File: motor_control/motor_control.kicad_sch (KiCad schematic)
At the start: 20 parts, among them J1 GPIO, J2 Conn_01x06_Pin, J3 Conn_01x06_Pin, SW1 PULLUP, SW2 PULLDOWN, SW4 SW_SPST, U1 HC-SR04

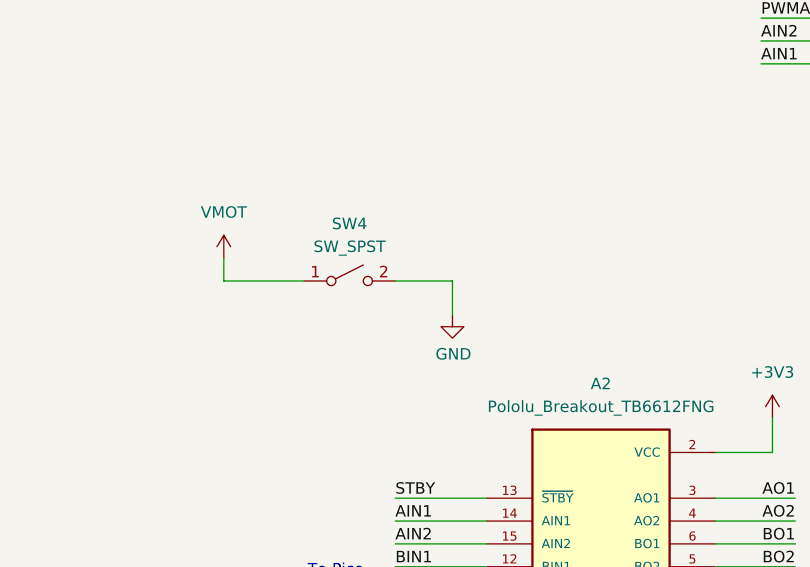
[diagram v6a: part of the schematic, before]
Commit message: replace tb6612 power switch with a 01x02 pin header
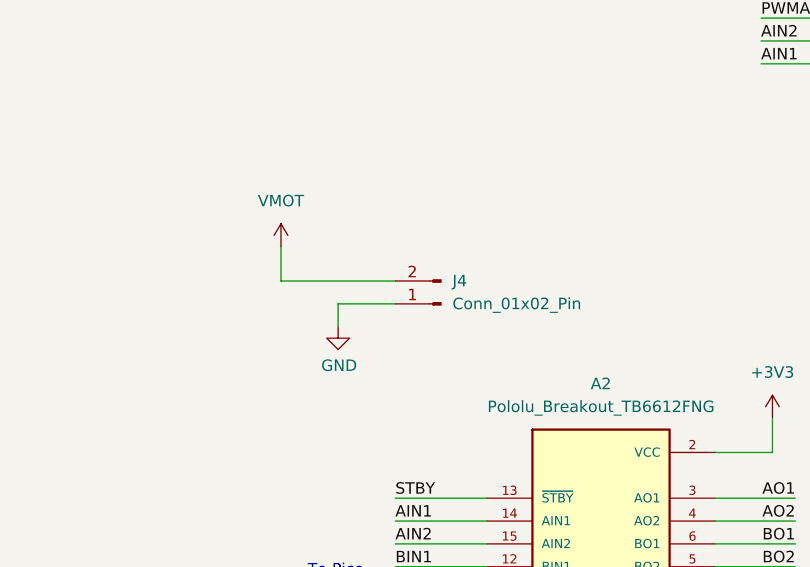
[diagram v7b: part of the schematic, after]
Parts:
- removed SW4: SW_SPST, symbol Switch:SW_SPST
- added J4: Conn_01x02_Pin, symbol Connector:Conn_01x02_Pin
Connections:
- net GND: now also J4.1 (Pin_1)
- net VMOT: now also J4.2 (Pin_2)
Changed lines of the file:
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@@
 	(wire
 		(pts
-			(xy 132.08 106.68) (xy 132.08 109.22)
-		)
-		(stroke
-			(width 0)
-			(type default)
-		)
-	)
-	(wire
-		(pts
 			(xy 76.2 50.8) (xy 76.2 63.5)
 		)
@@
 	(wire
 		(pts
+			(xy 151.13 111.76) (xy 144.78 111.76)
+		)
+		(stroke
+			(width 0)
+			(type default)
+		)
+	)
+	(wire
+		(pts
 			(xy 251.46 77.47) (xy 264.16 77.47)
 		)
@@
 	(wire
 		(pts
+			(xy 138.43 109.22) (xy 151.13 109.22)
+		)
+		(stroke
+			(width 0)
+			(type default)
+		)
+	)
+	(wire
+		(pts
 			(xy 142.24 151.13) (xy 161.29 151.13)
 		)
@@
 	(wire
 		(pts
+			(xy 144.78 111.76) (xy 144.78 114.3)
+		)
+		(stroke
+			(width 0)
+			(type default)
+		)
+	)
+	(wire
+		(pts
 			(xy 55.88 48.26) (xy 60.96 48.26)
 		)
@@
 	(wire
 		(pts
-			(xy 151.13 109.22) (xy 157.48 109.22)
-		)
-		(stroke
-			(width 0)
-			(type default)
-		)
-	)
-	(wire
-		(pts
-			(xy 157.48 109.22) (xy 157.48 113.03)
-		)
-		(stroke
-			(width 0)
-			(type default)
-		)
-	)
-	(wire
-		(pts
 			(xy 87.63 151.13) (xy 95.25 151.13)
 		)
@@
 	(wire
 		(pts
-			(xy 132.08 109.22) (xy 140.97 109.22)
-		)
-		(stroke
-			(width 0)
-			(type default)
-		)
-	)
-	(wire
-		(pts
 			(xy 31.75 53.34) (xy 60.96 53.34)
 		)
@@
 	(wire
 		(pts
+			(xy 138.43 105.41) (xy 138.43 109.22)
+		)
+		(stroke
+			(width 0)
+			(type default)
+		)
+	)
+	(wire
+		(pts
 			(xy 58.42 76.2) (xy 60.96 76.2)
 		)
@@
 	(symbol
 		(lib_id "power:+3V3")
-		(at 132.08 106.68 0)
-		(unit 1)
-		(exclude_from_sim no)
-		(in_bom yes)
-		(on_board yes)
-		(dnp no)
-		(fields_autoplaced yes)
-		(property "Reference" "#PWR021"
-			(at 132.08 110.49 0)
-			(effects
-				(font
-					(size 1.27 1.27)
-				)
-				(hide yes)
-			)
-		)
-		(property "Value" "VMOT"
-			(at 132.08 101.6 0)
-			(effects
-				(font
-					(size 1.27 1.27)
-				)
-			)
-		)
-		(property "Footprint" ""
-			(at 132.08 106.68 0)
-			(effects
-				(font
-					(size 1.27 1.27)
-				)
-				(hide yes)
-			)
-		)
-		(property "Datasheet" ""
-			(at 132.08 106.68 0)
-			(effects
-				(font
-					(size 1.27 1.27)
-				)
-				(hide yes)
-			)
-		)
-		(property "Description" "Power symbol creates a global label with name \"+3V3\""
-			(at 132.08 106.68 0)
-			(effects
-				(font
-					(size 1.27 1.27)
-				)
-				(hide yes)
-			)
-		)
-		(pin "1"
-		)
-		(instances
-			(project "motor_control"
-				(path "/e63e39d7-6ac0-4ffd-8aa3-1841a4541b55"
-					(reference "#PWR021")
-					(unit 1)
-				)
-			)
-		)
-	)
-	(symbol
-		(lib_id "power:+3V3")
 		(at 63.5 128.27 0)
 		(unit 1)
@@
 	)
 	(symbol
+		(lib_id "Connector:Conn_01x02_Pin")
+		(at 156.21 111.76 180)
+		(unit 1)
+		(exclude_from_sim no)
+		(in_bom yes)
+		(on_board yes)
+		(dnp no)
+		(fields_autoplaced yes)
+		(property "Reference" "J4"
+			(at 157.48 109.2199 0)
+			(effects
+				(font
+					(size 1.27 1.27)
+				)
+				(justify right)
+			)
+		)
+		(property "Value" "Conn_01x02_Pin"
+			(at 157.48 111.7599 0)
+			(effects
+				(font
+					(size 1.27 1.27)
+				)
+				(justify right)
+			)
+		)
+		(property "Footprint" ""
+			(at 156.21 111.76 0)
+			(effects
+				(font
+					(size 1.27 1.27)
+				)
+				(hide yes)
+			)
+		)
+		(property "Datasheet" "~"
+			(at 156.21 111.76 0)
+			(effects
+				(font
+					(size 1.27 1.27)
+				)
+				(hide yes)
+			)
+		)
+		(property "Description" "Generic connector, single row, 01x02, script generated"
+			(at 156.21 111.76 0)
+			(effects
+				(font
+					(size 1.27 1.27)
+				)
+				(hide yes)
+			)
+		)
+		(pin "1"
+		)
+		(pin "2"
+		)
+		(instances
+			(project ""
+				(path "/e63e39d7-6ac0-4ffd-8aa3-1841a4541b55"
+					(reference "J4")
+					(unit 1)
+				)
+			)
+		)
+	)
+	(symbol
 		(lib_id "Device:LED_RKGB")
 		(at 107.95 179.07 180)
@@
 	)
 	(symbol
-		(lib_id "power:+3V3")
-		(at 223.52 19.05 0)
+		(lib_id "power:GND")
+		(at 144.78 114.3 0)
 		(unit 1)
 		(exclude_from_sim no)
@@
 		(on_board yes)
 		(dnp no)
-		(fields_autoplaced yes)
-		(property "Reference" "#PWR014"
-			(at 223.52 22.86 0)
+		(property "Reference" "#PWR021"
+			(at 144.78 120.65 0)
 			(effects
 				(font
@@
 			)
 		)
-		(property "Value" "VSYS"
-			(at 223.52 13.97 0)
+		(property "Value" "GND"
+			(at 144.8943 118.6244 0)
 			(effects
 				(font
@@
 		)
 		(property "Footprint" ""
-			(at 223.52 19.05 0)
+			(at 144.78 114.3 0)
 			(effects
 				(font
 					(size 1.27 1.27)
 				)
-				(hide yes)
 			)
 		)
 		(property "Datasheet" ""
-			(at 223.52 19.05 0)
+			(at 144.78 114.3 0)
 			(effects
 				(font
 					(size 1.27 1.27)
 				)
-				(hide yes)
 			)
 		)
-		(property "Description" "Power symbol creates a global label with name \"+3V3\""
-			(at 223.52 19.05 0)
+		(property "Description" "Power symbol creates a global label with name \"GND\" , ground"
+			(at 144.78 114.3 0)
 			(effects
 				(font
@@
 			(project "motor_control"
 				(path "/e63e39d7-6ac0-4ffd-8aa3-1841a4541b55"
-					(reference "#PWR014")
+					(reference "#PWR021")
 					(unit 1)
 				)
@@
 	)
 	(symbol
-		(lib_id "Switch:SW_SPST")
-		(at 146.05 109.22 0)
+		(lib_id "power:+3V3")
+		(at 223.52 19.05 0)
 		(unit 1)
 		(exclude_from_sim no)
@@
 		(dnp no)
 		(fields_autoplaced yes)
-		(property "Reference" "SW4"
-			(at 146.05 102.87 0)
+		(property "Reference" "#PWR014"
+			(at 223.52 22.86 0)
 			(effects
 				(font
 					(size 1.27 1.27)
 				)
+				(hide yes)
 			)
 		)
-		(property "Value" "SW_SPST"
-			(at 146.05 105.41 0)
+		(property "Value" "VSYS"
+			(at 223.52 13.97 0)
 			(effects
 				(font
@@
 		)
 		(property "Footprint" ""
-			(at 146.05 109.22 0)
+			(at 223.52 19.05 0)
 			(effects
 				(font
@@
 			)
 		)
-		(property "Datasheet" "~"
-			(at 146.05 109.22 0)
+		(property "Datasheet" ""
+			(at 223.52 19.05 0)
 			(effects
 				(font
@@
 			)
 		)
-		(property "Description" "Single Pole Single Throw (SPST) switch"
-			(at 146.05 109.22 0)
+		(property "Description" "Power symbol creates a global label with name \"+3V3\""
+			(at 223.52 19.05 0)
 			(effects
 				(font
@@
 			)
 		)
-		(pin "2"
-		)
 		(pin "1"
 		)
 		(instances
-			(project ""
+			(project "motor_control"
 				(path "/e63e39d7-6ac0-4ffd-8aa3-1841a4541b55"
-					(reference "SW4")
+					(reference "#PWR014")
 					(unit 1)
 				)
@@
 	)
 	(symbol
-		(lib_id "power:GND")
-		(at 157.48 113.03 0)
+		(lib_id "power:+3V3")
+		(at 138.43 105.41 0)
 		(unit 1)
 		(exclude_from_sim no)
@@
 		(on_board yes)
 		(dnp no)
+		(fields_autoplaced yes)
 		(property "Reference" "#PWR019"
-			(at 157.48 119.38 0)
+			(at 138.43 109.22 0)
 			(effects
 				(font
@@
 			)
 		)
-		(property "Value" "GND"
-			(at 157.5943 117.3544 0)
+		(property "Value" "VMOT"
+			(at 138.43 100.33 0)
 			(effects
 				(font
@@
 		)
 		(property "Footprint" ""
-			(at 157.48 113.03 0)
+			(at 138.43 105.41 0)
 			(effects
 				(font
 					(size 1.27 1.27)
 				)
+				(hide yes)
 			)
 		)
 		(property "Datasheet" ""
-			(at 157.48 113.03 0)
+			(at 138.43 105.41 0)
 			(effects
 				(font
 					(size 1.27 1.27)
 				)
+				(hide yes)
 			)
 		)
-		(property "Description" "Power symbol creates a global label with name \"GND\" , ground"
-			(at 157.48 113.03 0)
+		(property "Description" "Power symbol creates a global label with name \"+3V3\""
+			(at 138.43 105.41 0)
 			(effects
 				(font

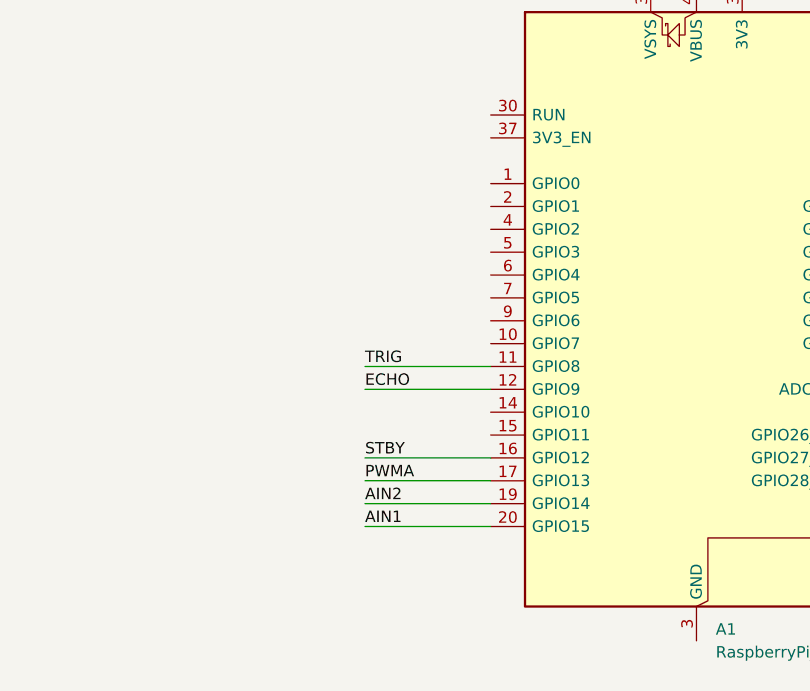
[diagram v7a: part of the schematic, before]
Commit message: add comm connections between pi and pico
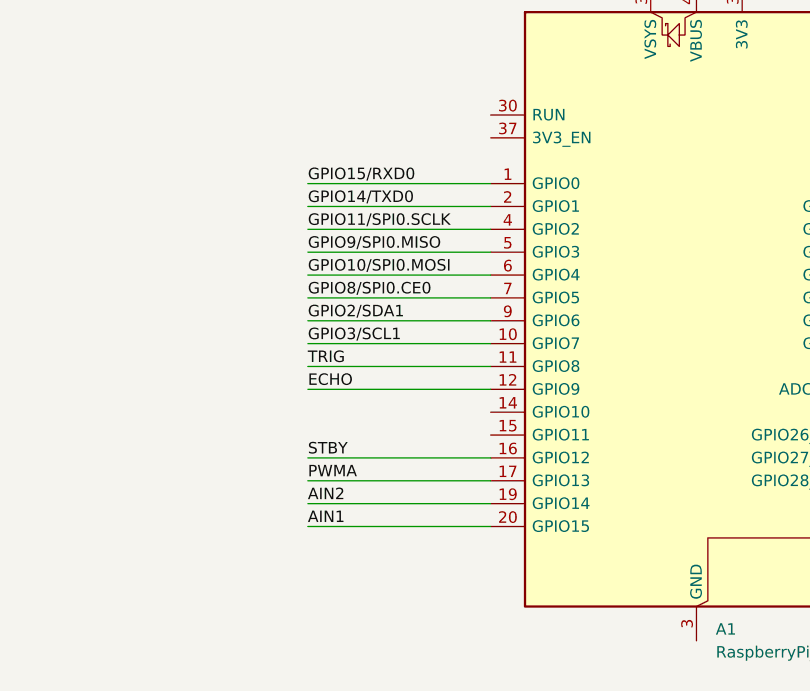
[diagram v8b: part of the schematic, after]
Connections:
- net GPIO10/SPI0.MOSI: now also A1.6 (GPIO4)
- net GPIO11/SPI0.SCLK: now also A1.4 (GPIO2)
- net GPIO14/TXD0: now also A1.2 (GPIO1)
- net GPIO15/RXD0: now also A1.1 (GPIO0)
- net GPIO2/SDA1: now also A1.9 (GPIO6)
- net GPIO3/SCL1: now also A1.10 (GPIO7)
- net GPIO8/SPI0.CE0: now also A1.7 (GPIO5)
- net GPIO9/SPI0.MISO: now also A1.5 (GPIO3)
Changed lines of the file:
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@@
+	(wire
+		(pts
+			(xy 185.42 64.77) (xy 205.74 64.77)
+		)
+		(stroke
+			(width 0)
+			(type default)
+		)
+	)
 	(wire
 		(pts
@@
 	(wire
 		(pts
+			(xy 185.42 82.55) (xy 205.74 82.55)
+		)
+		(stroke
+			(width 0)
+			(type default)
+		)
+	)
+	(wire
+		(pts
 			(xy 151.13 133.35) (xy 161.29 133.35)
 		)
@@
 	(wire
 		(pts
+			(xy 185.42 46.99) (xy 205.74 46.99)
+		)
+		(stroke
+			(width 0)
+			(type default)
+		)
+	)
+	(wire
+		(pts
 			(xy 41.91 151.13) (xy 41.91 153.67)
 		)
@@
 	(wire
 		(pts
+			(xy 185.42 67.31) (xy 205.74 67.31)
+		)
+		(stroke
+			(width 0)
+			(type default)
+		)
+	)
+	(wire
+		(pts
 			(xy 76.2 173.99) (xy 87.63 173.99)
 		)
@@
 	(wire
 		(pts
+			(xy 185.42 59.69) (xy 205.74 59.69)
+		)
+		(stroke
+			(width 0)
+			(type default)
+		)
+	)
+	(wire
+		(pts
 			(xy 55.88 24.13) (xy 55.88 27.94)
 		)
@@
 	(wire
 		(pts
+			(xy 185.42 77.47) (xy 205.74 77.47)
+		)
+		(stroke
+			(width 0)
+			(type default)
+		)
+	)
+	(wire
+		(pts
 			(xy 142.24 151.13) (xy 161.29 151.13)
 		)
@@
 	(wire
 		(pts
-			(xy 191.77 67.31) (xy 205.74 67.31)
-		)
-		(stroke
-			(width 0)
-			(type default)
-		)
-	)
-	(wire
-		(pts
 			(xy 31.75 33.02) (xy 60.96 33.02)
 		)
@@
 	(wire
 		(pts
+			(xy 185.42 54.61) (xy 205.74 54.61)
+		)
+		(stroke
+			(width 0)
+			(type default)
+		)
+	)
+	(wire
+		(pts
 			(xy 76.2 27.94) (xy 76.2 30.48)
 		)
@@
 	(wire
 		(pts
+			(xy 185.42 57.15) (xy 205.74 57.15)
+		)
+		(stroke
+			(width 0)
+			(type default)
+		)
+	)
+	(wire
+		(pts
 			(xy 33.02 165.1) (xy 33.02 168.91)
 		)
@@
 	(wire
 		(pts
+			(xy 185.42 80.01) (xy 205.74 80.01)
+		)
+		(stroke
+			(width 0)
+			(type default)
+		)
+	)
+	(wire
+		(pts
 			(xy 76.2 24.13) (xy 76.2 27.94)
 		)
@@
 	(wire
 		(pts
-			(xy 191.77 69.85) (xy 205.74 69.85)
-		)
-		(stroke
-			(width 0)
-			(type default)
-		)
-	)
-	(wire
-		(pts
 			(xy 76.2 27.94) (xy 73.66 27.94)
 		)
@@
 	(wire
 		(pts
+			(xy 185.42 62.23) (xy 205.74 62.23)
+		)
+		(stroke
+			(width 0)
+			(type default)
+		)
+	)
+	(wire
+		(pts
 			(xy 31.75 53.34) (xy 60.96 53.34)
 		)
@@
 	(wire
 		(pts
-			(xy 191.77 82.55) (xy 205.74 82.55)
-		)
-		(stroke
-			(width 0)
-			(type default)
-		)
-	)
-	(wire
-		(pts
 			(xy 31.75 66.04) (xy 60.96 66.04)
 		)
@@
 	(wire
 		(pts
+			(xy 185.42 49.53) (xy 205.74 49.53)
+		)
+		(stroke
+			(width 0)
+			(type default)
+		)
+	)
+	(wire
+		(pts
 			(xy 251.46 74.93) (xy 264.16 74.93)
 		)
@@
 	(wire
 		(pts
+			(xy 185.42 85.09) (xy 205.74 85.09)
+		)
+		(stroke
+			(width 0)
+			(type default)
+		)
+	)
+	(wire
+		(pts
 			(xy 186.69 135.89) (xy 195.58 135.89)
 		)
@@
 	(wire
 		(pts
-			(xy 191.77 77.47) (xy 205.74 77.47)
-		)
-		(stroke
-			(width 0)
-			(type default)
-		)
-	)
-	(wire
-		(pts
 			(xy 168.91 21.59) (xy 168.91 25.4)
 		)
@@
 	(wire
 		(pts
-			(xy 191.77 80.01) (xy 205.74 80.01)
-		)
-		(stroke
-			(width 0)
-			(type default)
-		)
-	)
-	(wire
-		(pts
 			(xy 142.24 148.59) (xy 142.24 151.13)
 		)
@@
 	(wire
 		(pts
+			(xy 185.42 69.85) (xy 205.74 69.85)
+		)
+		(stroke
+			(width 0)
+			(type default)
+		)
+	)
+	(wire
+		(pts
 			(xy 63.5 128.27) (xy 63.5 133.35)
 		)
@@
 	(wire
 		(pts
+			(xy 185.42 52.07) (xy 205.74 52.07)
+		)
+		(stroke
+			(width 0)
+			(type default)
+		)
+	)
+	(wire
+		(pts
 			(xy 76.2 184.15) (xy 87.63 184.15)
 		)
@@
 		)
 	)
-	(wire
-		(pts
-			(xy 191.77 85.09) (xy 205.74 85.09)
-		)
-		(stroke
-			(width 0)
-			(type default)
+	(label "GPIO8{slash}SPI0.CE0"
+		(at 185.42 59.69 0)
+		(effects
+			(font
+				(size 1.27 1.27)
+			)
+			(justify left bottom)
 		)
 	)
@@
 		)
 	)
+	(label "GPIO10{slash}SPI0.MOSI"
+		(at 185.42 57.15 0)
+		(effects
+			(font
+				(size 1.27 1.27)
+			)
+			(justify left bottom)
+		)
+	)
 	(label "STBY"
 		(at 151.13 133.35 0)
@@
 	)
 	(label "AIN2"
-		(at 191.77 82.55 0)
+		(at 185.42 82.55 0)
 		(effects
 			(font
@@
 	)
 	(label "STBY"
-		(at 191.77 77.47 0)
+		(at 185.42 77.47 0)
 		(effects
 			(font
@@
 		)
 	)
+	(label "GPIO11{slash}SPI0.SCLK"
+		(at 185.42 52.07 0)
+		(effects
+			(font
+				(size 1.27 1.27)
+			)
+			(justify left bottom)
+		)
+	)
 	(label "TRIG"
 		(at 86.36 148.59 0)
@@
 		)
 	)
+	(label "GPIO3{slash}SCL1"
+		(at 185.42 64.77 0)
+		(effects
+			(font
+				(size 1.27 1.27)
+			)
+			(justify left bottom)
+		)
+	)
 	(label "PULLUP"
 		(at 264.16 62.23 180)
@@
 		)
 	)
+	(label "GPIO14{slash}TXD0"
+		(at 185.42 49.53 0)
+		(effects
+			(font
+				(size 1.27 1.27)
+			)
+			(justify left bottom)
+		)
+	)
 	(label "BIN1"
 		(at 264.16 49.53 180)
@@
 		)
 	)
+	(label "GPIO15{slash}RXD0"
+		(at 185.42 46.99 0)
+		(effects
+			(font
+				(size 1.27 1.27)
+			)
+			(justify left bottom)
+		)
+	)
 	(label "GPIO2{slash}SDA1"
 		(at 31.75 30.48 0)
@@
 	)
 	(label "ECHO"
-		(at 191.77 69.85 0)
+		(at 185.42 69.85 0)
 		(effects
 			(font
@@
 	)
 	(label "PWMA"
-		(at 191.77 80.01 0)
+		(at 185.42 80.01 0)
 		(effects
 			(font
@@
 		)
 	)
+	(label "GPIO9{slash}SPI0.MISO"
+		(at 185.42 54.61 0)
+		(effects
+			(font
+				(size 1.27 1.27)
+			)
+			(justify left bottom)
+		)
+	)
 	(label "GPIO7{slash}SPI0.CE1"
 		(at 100.33 58.42 180)
@@
 		)
 	)
+	(label "GPIO2{slash}SDA1"
+		(at 185.42 62.23 0)
+		(effects
+			(font
+				(size 1.27 1.27)
+			)
+			(justify left bottom)
+		)
+	)
 	(label "RED"
 		(at 264.16 80.01 180)
@@
 	)
 	(label "AIN1"
-		(at 191.77 85.09 0)
+		(at 185.42 85.09 0)
 		(effects
 			(font
@@
 	)
 	(label "TRIG"
-		(at 191.77 67.31 0)
-		(effects
-			(font
+		(at 185.42 67.31 0)
+		(effects
+			(font
